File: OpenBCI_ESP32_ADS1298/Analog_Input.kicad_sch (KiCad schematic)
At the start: 49 parts, among them J1 Conn_02x13_Odd_Even, U1 TPD4E1B06, U2 TPD4E1B06, U3 TPD4E1B06, U4 TPD4E1B06, U5 TPD4E1B06, U6 TPD4E1B06

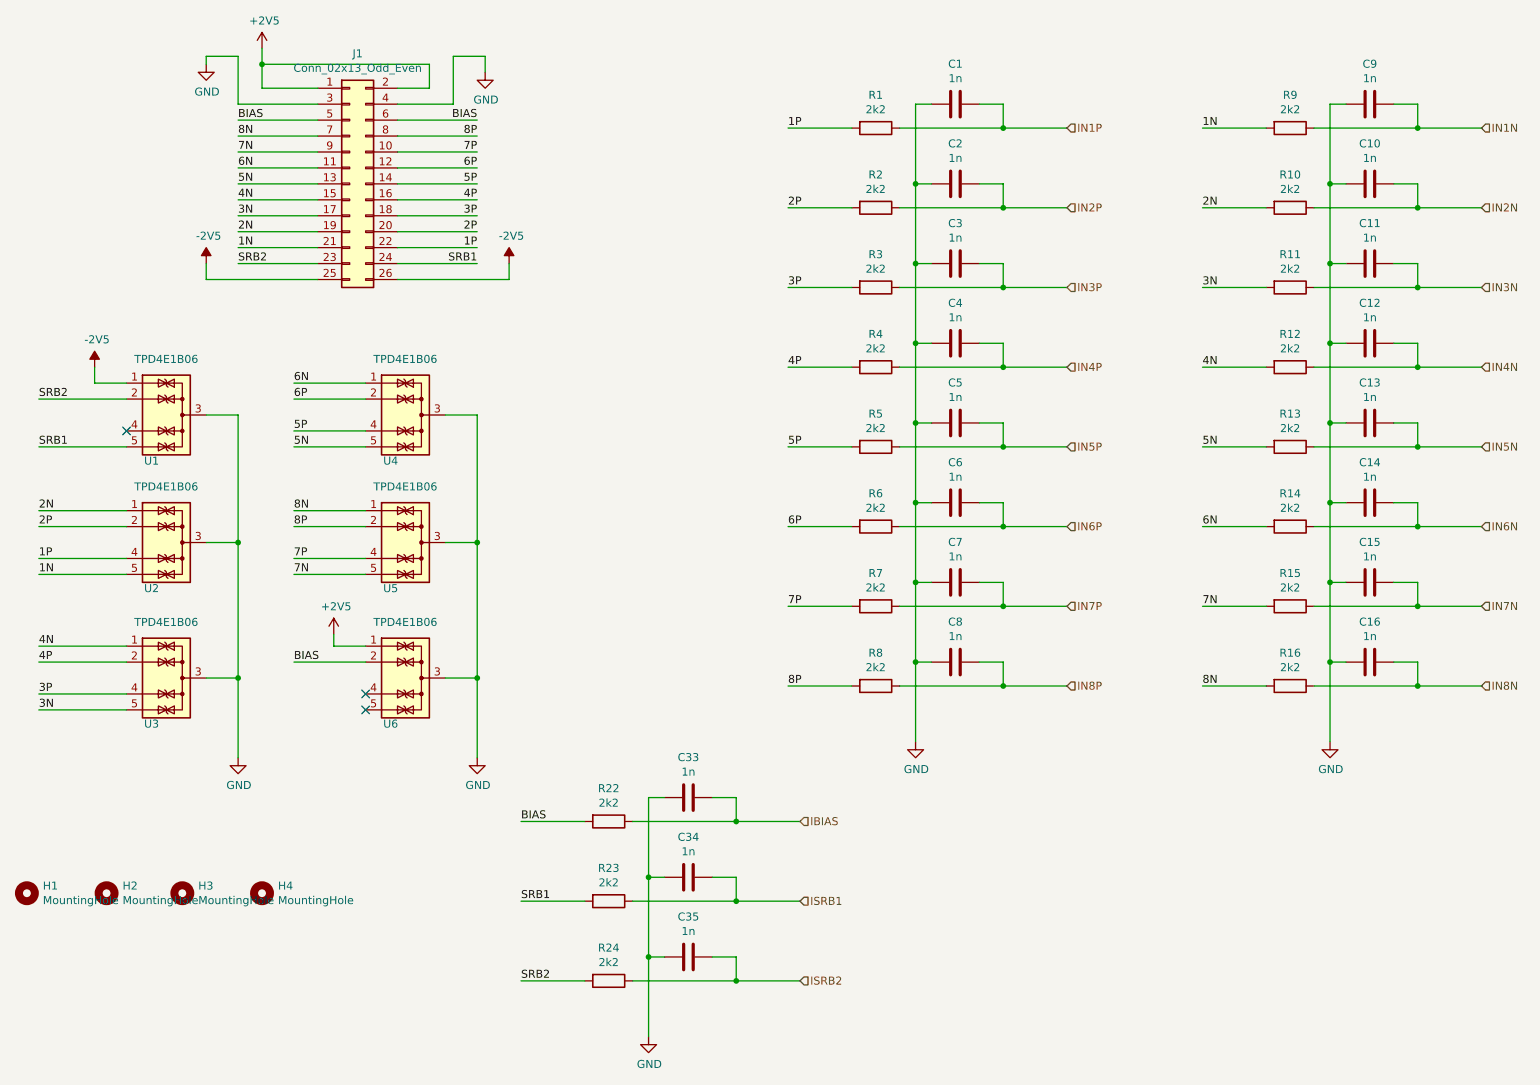
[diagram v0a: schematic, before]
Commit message: add ADS1298 files
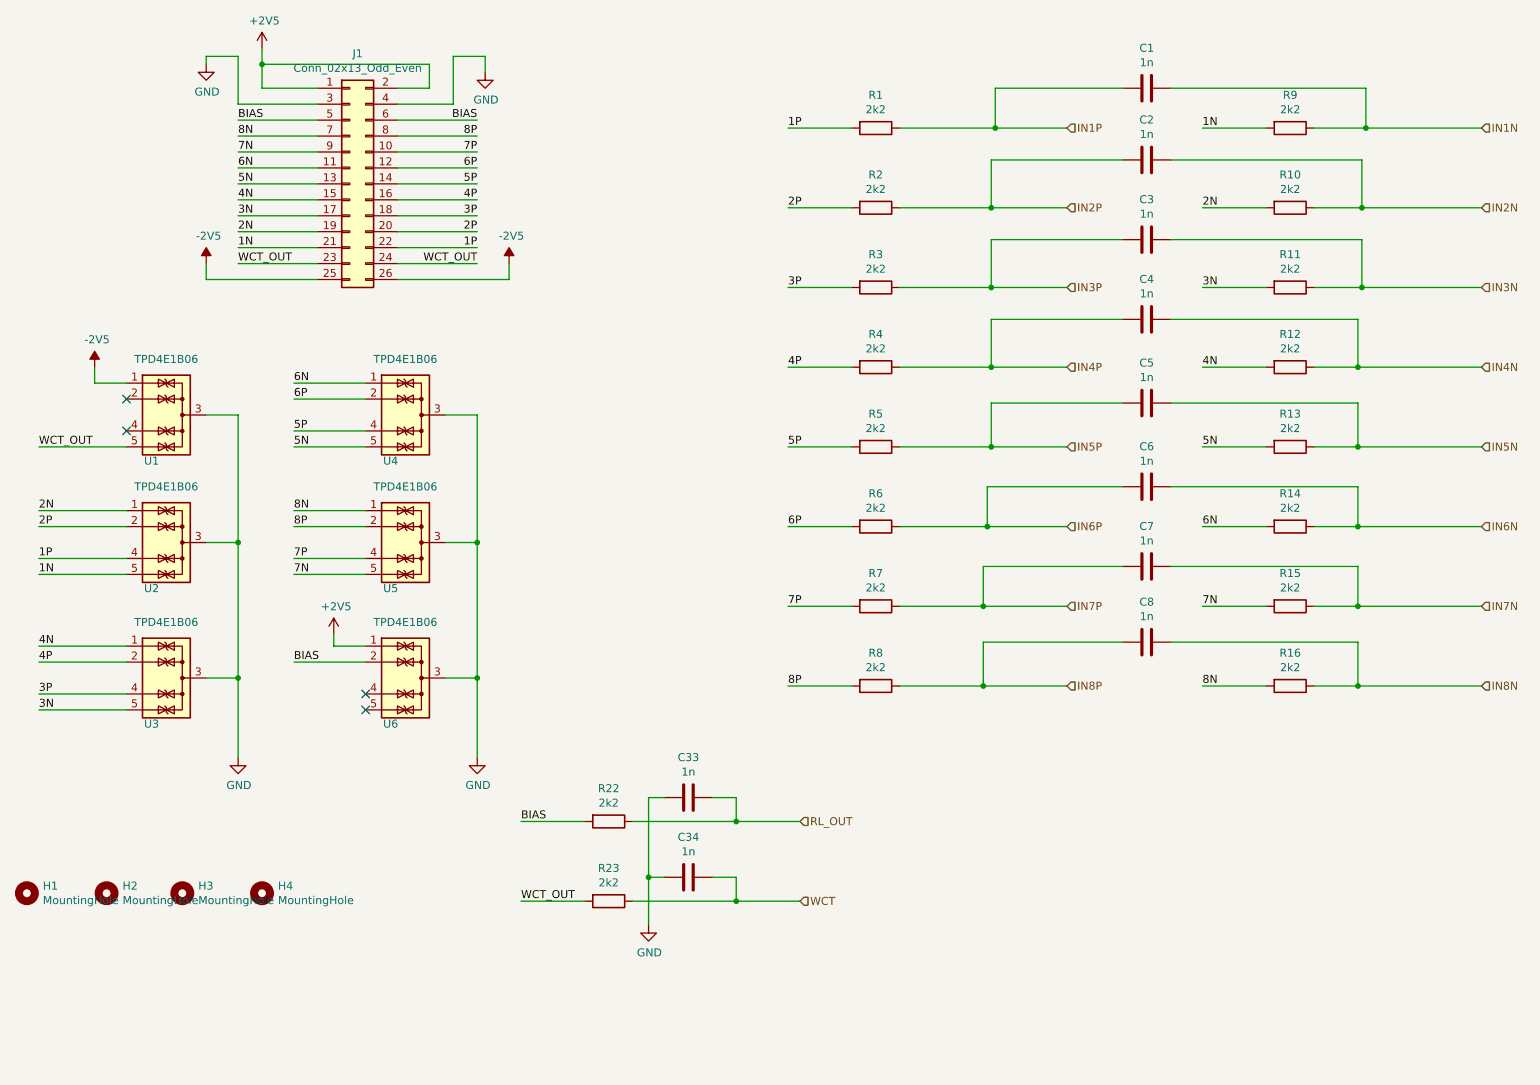
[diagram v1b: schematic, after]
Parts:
- removed C10, C11, C12, C13, C14, C15, C16, C35, C9: 1n, Capacitor_SMD:C_0603_1608Metric, symbol Device:C
- removed R24: 2k2, Resistor_SMD:R_0603_1608Metric, symbol Device:R
- U1, U2, U3, U4, U5, U6: footprint Package_TO_SOT_SMD:SOT-23-6 -> Package_TO_SOT_SMD:SOT-363_SC-70-6
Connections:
- net GND: no longer C1.2, C2.2, C3.2, C4.2, C5.2, C6.2, C7.2, C8.2
- net IN1N: now also C1.1
- net IN1P: now also C1.2; no longer C1.1
- net IN2N: now also C2.1
- net IN2P: now also C2.2; no longer C2.1
- net IN3N: now also C3.1
- net IN3P: now also C3.2; no longer C3.1
- net IN4N: now also C4.1
- net IN4P: now also C4.2; no longer C4.1
- net IN5N: now also C5.1
- net IN5P: now also C5.2; no longer C5.1
- net IN6N: now also C6.1
- net IN6P: now also C6.2; no longer C6.1
- net IN7N: now also C7.1
- net IN7P: now also C7.2; no longer C7.1
- net IN8N: now also C8.1
- net IN8P: now also C8.2; no longer C8.1
- net IBIAS renamed RL_OUT
- net ISRB1 renamed WCT
- net SRB1 renamed WCT_OUT
- net WCT_OUT: now also J1.23 (Pin_23)
- net SRB2: no longer names the net of U1.2 (IO2)
- net SRB2: no longer J1.23 (Pin_23)
- no-connect marks 3 -> 4
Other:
- moved on the sheet: C1, C2, C3, C4, C5, C6, C7, C8

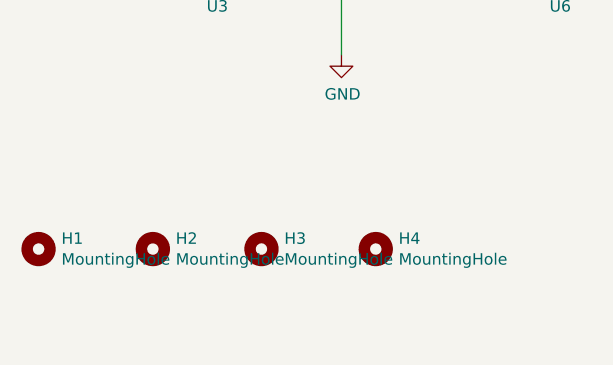
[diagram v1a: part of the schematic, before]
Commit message: Fix ADS1298 Mounting Holes
Fix ADS1298R Mounting holes shorting layers
Add some ADS1298R Arduino Files
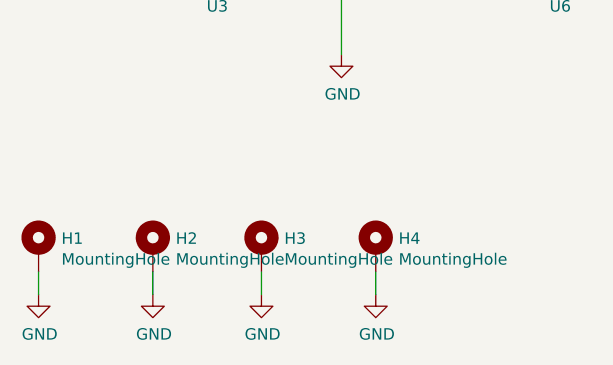
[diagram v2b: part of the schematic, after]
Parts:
- H1, H2, H3, H4: footprint MountingHole:MountingHole_2.7mm_M2.5 -> MountingHole:MountingHole_2.7mm_M2.5_DIN965_Pad_TopBottom; symbol Mechanical:MountingHole -> Mechanical:MountingHole_Pad
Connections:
- net GND: now also H1.1, H2.1, H3.1, H4.1
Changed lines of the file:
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@@
+    (stroke (width 0) (type default))
+  )
+  (wire (pts (xy 69.85 163.83) (xy 69.85 166.37))
     (stroke (width 0) (type default))
   )
@@
     (stroke (width 0) (type default))
   )
+  (wire (pts (xy 45.085 163.83) (xy 45.085 166.37))
+    (stroke (width 0) (type default))
+  )
   (wire (pts (xy 86.36 121.92) (xy 81.28 121.92))
     (stroke (width 0) (type default))
@@
     (stroke (width 0) (type default))
   )
+  (wire (pts (xy 57.15 163.83) (xy 57.15 166.37))
+    (stroke (width 0) (type default))
+  )
   (wire (pts (xy 104.14 85.09) (xy 104.14 105.41))
     (stroke (width 0) (type default))
@@
   )
   (wire (pts (xy 91.44 53.34) (xy 104.14 53.34))
+    (stroke (width 0) (type default))
+  )
+  (wire (pts (xy 32.385 163.83) (xy 32.385 166.37))
     (stroke (width 0) (type default))
   )
@@
     )
   )
-  (symbol (lib_id "Mechanical:MountingHole") (at 32.385 161.29 0) (unit 1)
+  (symbol (lib_id "Mechanical:MountingHole_Pad") (at 32.385 161.29 0) (unit 1)
     (in_bom yes) (on_board yes) (dnp no)
     (property "Reference" "H1" (at 34.925 160.1216 0)
@@
       (effects (font (size 1.27 1.27)) (justify left))
     )
-    (property "Footprint" "MountingHole:MountingHole_2.7mm_M2.5" (at 32.385 161.29 0)
+    (property "Footprint" "MountingHole:MountingHole_2.7mm_M2.5_DIN965_Pad_TopBottom" (at 32.385 161.29 0)
       (effects (font (size 1.27 1.27)) hide)
     )
@@
       (effects (font (size 1.27 1.27)) hide)
     )
+    (pin "1")
     (instances
       (project "OpenBCI_ESP32_ADS1298"
@@
     )
   )
-  (symbol (lib_id "Mechanical:MountingHole") (at 45.085 161.29 0) (unit 1)
+  (symbol (lib_id "Mechanical:MountingHole_Pad") (at 45.085 161.29 0) (unit 1)
     (in_bom yes) (on_board yes) (dnp no)
     (property "Reference" "H2" (at 47.625 160.1216 0)
@@
       (effects (font (size 1.27 1.27)) (justify left))
     )
-    (property "Footprint" "MountingHole:MountingHole_2.7mm_M2.5" (at 45.085 161.29 0)
+    (property "Footprint" "MountingHole:MountingHole_2.7mm_M2.5_DIN965_Pad_TopBottom" (at 45.085 161.29 0)
       (effects (font (size 1.27 1.27)) hide)
     )
@@
       (effects (font (size 1.27 1.27)) hide)
     )
+    (pin "1")
     (instances
       (project "OpenBCI_ESP32_ADS1298"
@@
     )
   )
-  (symbol (lib_id "Mechanical:MountingHole") (at 57.15 161.29 0) (unit 1)
+  (symbol (lib_id "Mechanical:MountingHole_Pad") (at 57.15 161.29 0) (unit 1)
     (in_bom yes) (on_board yes) (dnp no)
     (property "Reference" "H3" (at 59.69 160.1216 0)
@@
       (effects (font (size 1.27 1.27)) (justify left))
     )
-    (property "Footprint" "MountingHole:MountingHole_2.7mm_M2.5" (at 57.15 161.29 0)
+    (property "Footprint" "MountingHole:MountingHole_2.7mm_M2.5_DIN965_Pad_TopBottom" (at 57.15 161.29 0)
       (effects (font (size 1.27 1.27)) hide)
     )
@@
       (effects (font (size 1.27 1.27)) hide)
     )
+    (pin "1")
     (instances
       (project "OpenBCI_ESP32_ADS1298"
@@
     )
   )
-  (symbol (lib_id "Mechanical:MountingHole") (at 69.85 161.29 0) (unit 1)
+  (symbol (lib_id "Mechanical:MountingHole_Pad") (at 69.85 161.29 0) (unit 1)
     (in_bom yes) (on_board yes) (dnp no)
     (property "Reference" "H4" (at 72.39 160.1216 0)
@@
       (effects (font (size 1.27 1.27)) (justify left))
     )
-    (property "Footprint" "MountingHole:MountingHole_2.7mm_M2.5" (at 69.85 161.29 0)
+    (property "Footprint" "MountingHole:MountingHole_2.7mm_M2.5_DIN965_Pad_TopBottom" (at 69.85 161.29 0)
       (effects (font (size 1.27 1.27)) hide)
     )
@@
       (effects (font (size 1.27 1.27)) hide)
     )
+    (pin "1")
     (instances
       (project "OpenBCI_ESP32_ADS1298"
@@
         )
       )
+    )
+  )
+  (symbol (lib_id "power:GND") (at 57.15 166.37 0) (unit 1)
+    (in_bom yes) (on_board yes) (dnp no)
+    (property "Reference" "#PWR029" (at 57.15 172.72 0)
+      (effects (font (size 1.27 1.27)) hide)
+    )
+    (property "Value" "GND" (at 57.277 170.7642 0)
+      (effects (font (size 1.27 1.27)))
+    )
+    (property "Footprint" "" (at 57.15 166.37 0)
+      (effects (font (size 1.27 1.27)) hide)
+    )
+    (property "Datasheet" "" (at 57.15 166.37 0)
+      (effects (font (size 1.27 1.27)) hide)
+    )
+    (pin "1")
+    (instances
+      (project "OpenBCI_ESP32_ADS1298"
+        (path "/c05ecaff-48cd-4ff1-bf9c-1e68fad43fda/00000000-0000-0000-0000-00006197b661"
+          (reference "#PWR029") (unit 1)
+        )
+      )
+    )
+  )
+  (symbol (lib_id "power:GND") (at 45.085 166.37 0) (unit 1)
+    (in_bom yes) (on_board yes) (dnp no)
+    (property "Reference" "#PWR028" (at 45.085 172.72 0)
+      (effects (font (size 1.27 1.27)) hide)
+    )
+    (property "Value" "GND" (at 45.212 170.7642 0)
+      (effects (font (size 1.27 1.27)))
+    )
+    (property "Footprint" "" (at 45.085 166.37 0)
+      (effects (font (size 1.27 1.27)) hide)
+    )
+    (property "Datasheet" "" (at 45.085 166.37 0)
+      (effects (font (size 1.27 1.27)) hide)
+    )
+    (pin "1")
+    (instances
+      (project "OpenBCI_ESP32_ADS1298"
+        (path "/c05ecaff-48cd-4ff1-bf9c-1e68fad43fda/00000000-0000-0000-0000-00006197b661"
+          (reference "#PWR028") (unit 1)
+        )
+      )
+    )
+  )
+  (symbol (lib_id "power:GND") (at 69.85 166.37 0) (unit 1)
+    (in_bom yes) (on_board yes) (dnp no)
+    (property "Reference" "#PWR030" (at 69.85 172.72 0)
+      (effects (font (size 1.27 1.27)) hide)
+    )
+    (property "Value" "GND" (at 69.977 170.7642 0)
+      (effects (font (size 1.27 1.27)))
+    )
+    (property "Footprint" "" (at 69.85 166.37 0)
+      (effects (font (size 1.27 1.27)) hide)
+    )
+    (property "Datasheet" "" (at 69.85 166.37 0)
+      (effects (font (size 1.27 1.27)) hide)
+    )
+    (pin "1")
+    (instances
+      (project "OpenBCI_ESP32_ADS1298"
+        (path "/c05ecaff-48cd-4ff1-bf9c-1e68fad43fda/00000000-0000-0000-0000-00006197b661"
+          (reference "#PWR030") (unit 1)
+        )
+      )
+    )
+  )
+  (symbol (lib_id "power:GND") (at 32.385 166.37 0) (unit 1)
+    (in_bom yes) (on_board yes) (dnp no)
+    (property "Reference" "#PWR027" (at 32.385 172.72 0)
+      (effects (font (size 1.27 1.27)) hide)
+    )
+    (property "Value" "GND" (at 32.512 170.7642 0)
+      (effects (font (size 1.27 1.27)))
+    )
+    (property "Footprint" "" (at 32.385 166.37 0)
+      (effects (font (size 1.27 1.27)) hide)
+    )
+    (property "Datasheet" "" (at 32.385 166.37 0)
+      (effects (font (size 1.27 1.27)) hide)
+    )
+    (pin "1")
+    (instances
+      (project "OpenBCI_ESP32_ADS1298"
+        (path "/c05ecaff-48cd-4ff1-bf9c-1e68fad43fda/00000000-0000-0000-0000-00006197b661"
+          (reference "#PWR027") (unit 1)
+        )
+      )
